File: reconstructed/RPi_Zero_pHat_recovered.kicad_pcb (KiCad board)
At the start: 2 copper layers, 65 x 30 mm, 85 parts

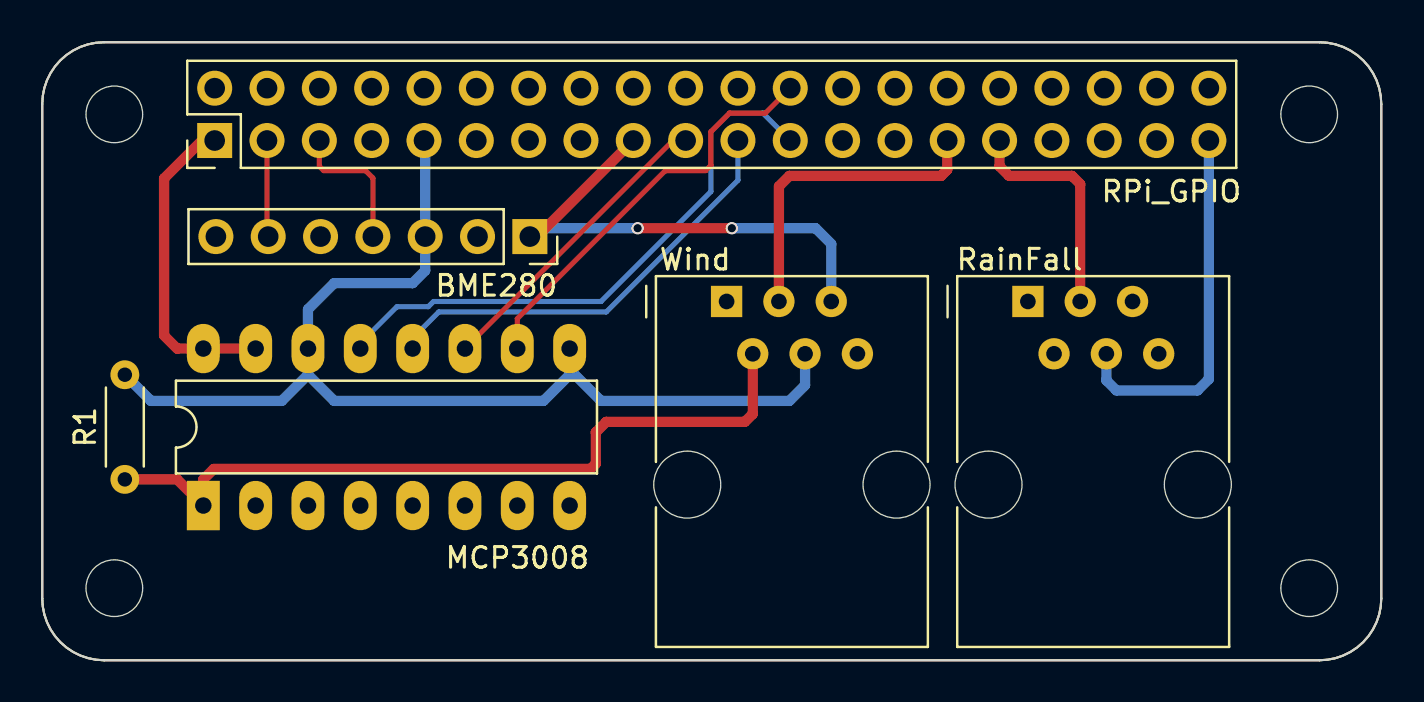
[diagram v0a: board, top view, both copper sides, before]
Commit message: Recover netlist and refdes onto the board; fix mounting-hole mask openings
The .kicad_pcb now carries components with reference designators, numbered
pads, and the recovered netlist on pads/tracks/vias - it opens with a
ratsnest and passes connectivity DRC. Mounting-hole soldermask openings are
taken from the mask gerbers (the 6.2mm keep-out rings were previously lost).
Board outline is no longer duplicated onto the copper layers.
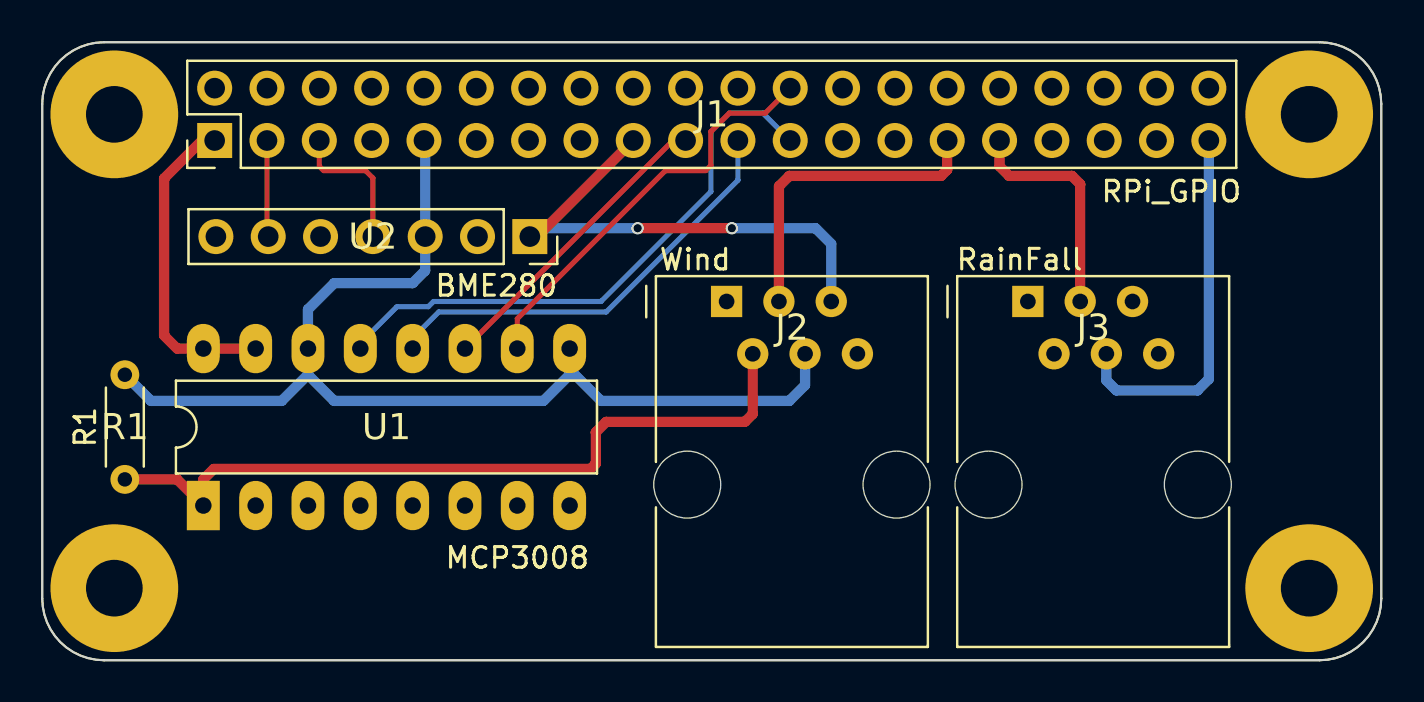
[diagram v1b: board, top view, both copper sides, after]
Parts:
- removed ? (x85): , 
- added H1: , , F.Cu at (74.0, 28.0)
- added H2: , , F.Cu at (16.0, 28.0)
- added H3: , , F.Cu at (74.0, 51.0)
- added H4: , , F.Cu at (16.0, 51.0)
- added H5: , , F.Cu at (58.4, 46.0)
- added H6: , , F.Cu at (68.6, 46.0)
- added H7: , , F.Cu at (43.8, 46.0)
- added H8: , , F.Cu at (54.0, 46.0)
- added J1: RPi_GPIO, , F.Cu at (45.0, 28.0)
- added J2: Wind, , F.Cu at (48.9, 38.4)
- added J3: RainFall, , F.Cu at (63.5, 38.4)
- added R1: 5k, , F.Cu at (16.5, 43.2)
- added U1: MCP3008, , F.Cu at (29.2, 43.2)
- added U2: BME280, , F.Cu at (28.5, 33.9)
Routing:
- net (no net): track 646.2 -> 0.66 mm, vias 2 -> 0
- net GND: track 0.00 -> 75.3 mm
- net +3V3: track 0.00 -> 41.2 mm, vias 0 -> 2
- net WIND_DIR: track 0.00 -> 37.4 mm
- net SPI_SCLK: track 0.00 -> 28.0 mm
- net SPI_MISO: track 0.00 -> 21.4 mm
- net SPI_CE0: track 0.00 -> 20.3 mm
- net WIND_SPD: track 0.00 -> 15.5 mm
- net SPI_MOSI: track 0.00 -> 14.9 mm
- net RAIN: track 0.00 -> 11.2 mm
- net I2C_SCL: track 0.00 -> 6.93 mm
- net I2C_SDA: track 0.00 -> 4.69 mm

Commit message: Fix RJ jack pin numbering: pads are staggered, not row-major
The modular-jack footprint numbers pins across the connector (1.27mm in x)
with odd pins in one row and even in the other, not row-major. With the
correct numbering Wind lands on pins 2-5 (a 6P4C plug) and RainFall on the
centre pair 3-4 (6P2C) - contiguous, as real modular plugs require. The
previous numbering put +3V3 on the anemometer common, so a cable built from
it would have shorted 3V3 to ground.

Adds a jack pinout table to the README.
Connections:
- J2 pad 2: WIND_SPD -> WIND_DIR
- J2 pad 3: +3V3 -> WIND_SPD
- J2 pad 4: WIND_DIR -> GND
- J2 pad 5: GND -> +3V3
- J3 pad 2: RAIN -> (no net)
- J3 pad 3: (no net) -> RAIN
- J3 pad 4: (no net) -> GND
- J3 pad 5: GND -> (no net)
